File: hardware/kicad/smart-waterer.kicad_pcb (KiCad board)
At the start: 2 copper layers, 180 x 120 mm, 16 parts, among them J1 USB-C, J2 土壤湿度, J3 水位检测, J4 水泵, J5 NTC, Q1 AO4606, U1 ESP32-C3-SuperMini, U2 XC6206-3.3V, U3 TP4056, U4 MT3608

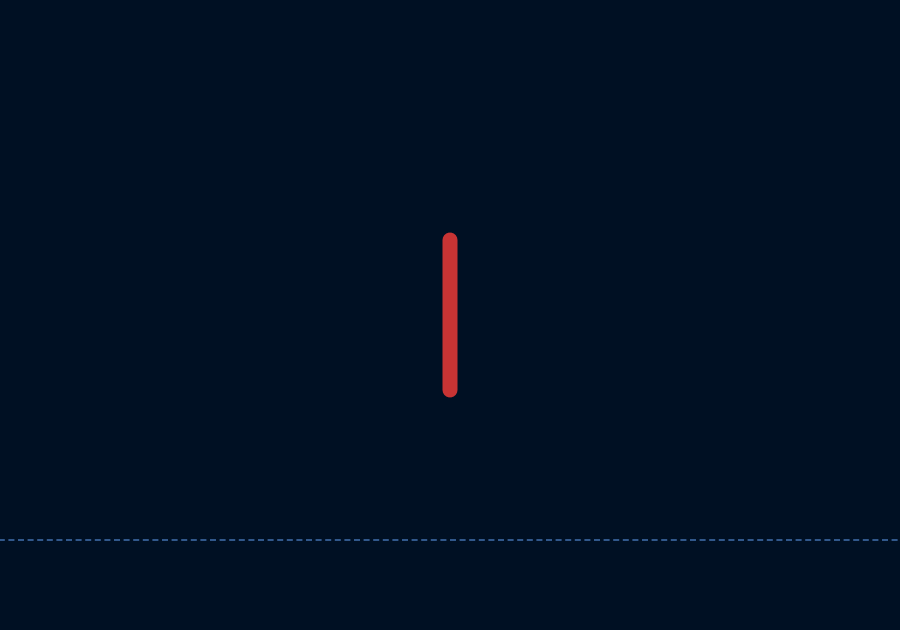
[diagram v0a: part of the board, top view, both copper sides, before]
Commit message: fix: 修复 KiCad 文件格式错误
修复:
- 修复 .kicad_sch 文件格式（正确的 S-Expr 格式）
- 修复 .kicad_pcb 文件格式（正确的 KiCad 9.0 格式）

问题:
- 之前生成的文件格式不正确
- KiCad 无法打开

现在:
- 符合 KiCad 9.0 格式规范
- 可以直接用 KiCad 打开
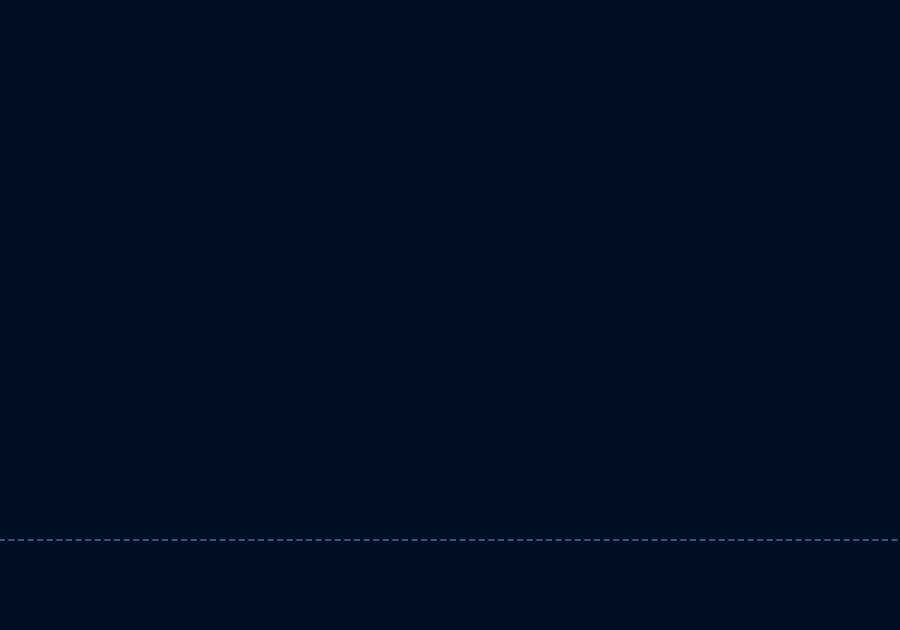
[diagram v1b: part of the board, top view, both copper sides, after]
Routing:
- net GND: track 5.00 -> 0.00 mm
